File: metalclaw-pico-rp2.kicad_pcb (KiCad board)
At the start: 4 copper layers, 21 x 51 mm, 122 parts, among them J1 USB4105-GF-A, J2 FTSH-105-01-L-DV-K, SW1 PTS810SJM250SMTR LFS, SW2 PTS810SJM250SMTR LFS, U1 XC6220B331MR-G, U2 RP2354B, U3 APS6404L-3SQR-SN, Y1 ABM8-272-T3

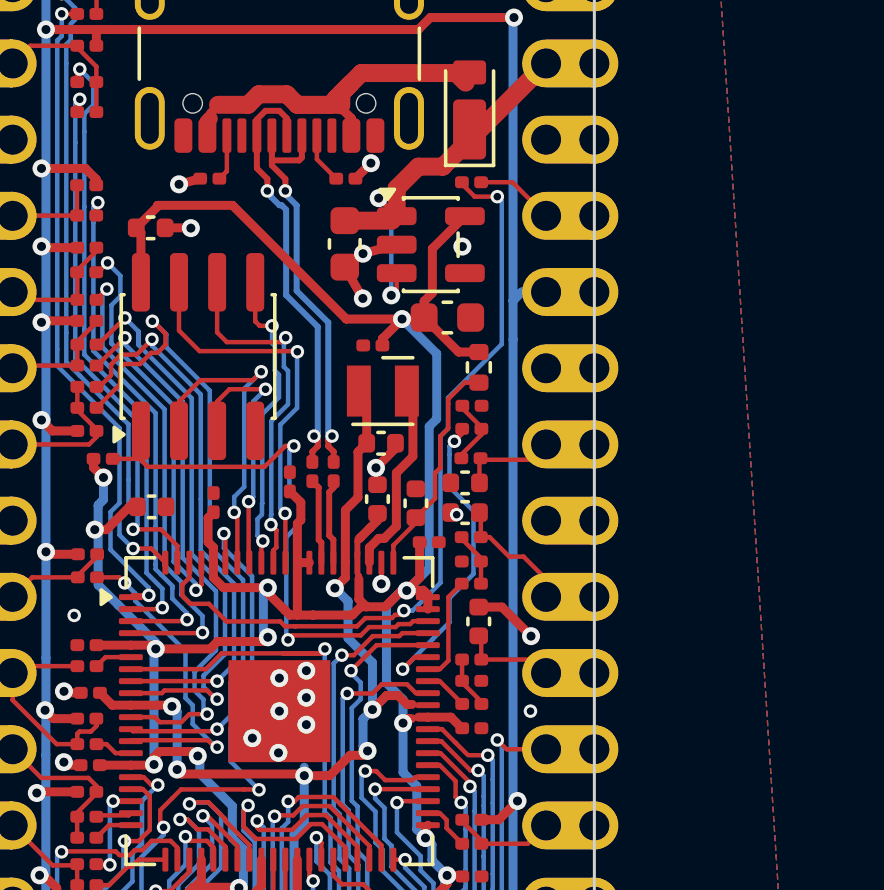
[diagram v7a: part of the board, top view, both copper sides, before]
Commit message: Add decoupling for pin 51
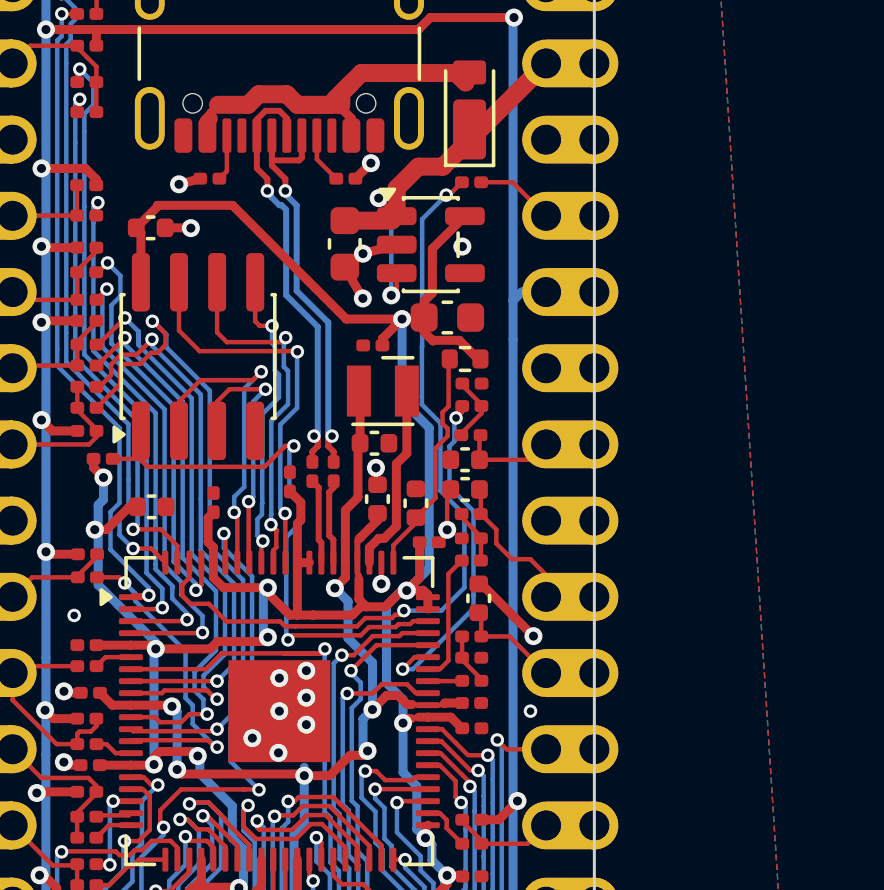
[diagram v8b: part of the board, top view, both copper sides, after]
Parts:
- added C29: 100n, Capacitor_SMD:C_0201_0603Metric, F.Cu at (170.2, 98.6)
- moved C4 0.77 mm to (170.0, 90.5)
- moved R26 0.77 mm to (170.2, 96.4)
- moved R31 0.77 mm to (170.2, 93.8)
- moved C5 0.77 mm to (170.0, 91.5)
- moved C6 0.77 mm to (170.5, 95.1)
- moved C7 0.77 mm to (170.2, 97.1)
- moved C8 0.77 mm to (170.2, 93.1)
- moved R23 0.77 mm to (170.2, 89.7)
- moved R24 0.77 mm to (170.2, 92.3)
- moved R30 0.77 mm to (170.2, 97.9)
- moved R32 0.76 mm to (170.2, 88.7)
- moved C9 0.74 mm to (170.2, 88.0)
- moved R73 0.54 mm to (170.0, 87.1), turned to 180 degrees
- moved C13 0.22 mm to (167.0, 89.9)
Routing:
- net Net-(U2-VREG_FB): track 34.3 -> 36.0 mm
- net /GP28: track 10.5 -> 11.7 mm
- net GND: track 23.1 -> 23.9 mm
- net /GP27: track 3.55 -> 4.32 mm
- net Net-(A1-GPIO27_ADC1): track 4.18 -> 4.92 mm
- net +3V3: track 118.6 -> 119.2 mm
